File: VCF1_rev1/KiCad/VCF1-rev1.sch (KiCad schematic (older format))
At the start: 40 parts, among them U1 Opamp_Dual_Generic, U2 Opamp_Dual_Generic, U3 74HC4053, U4 CEM3350, U5 74HC4053

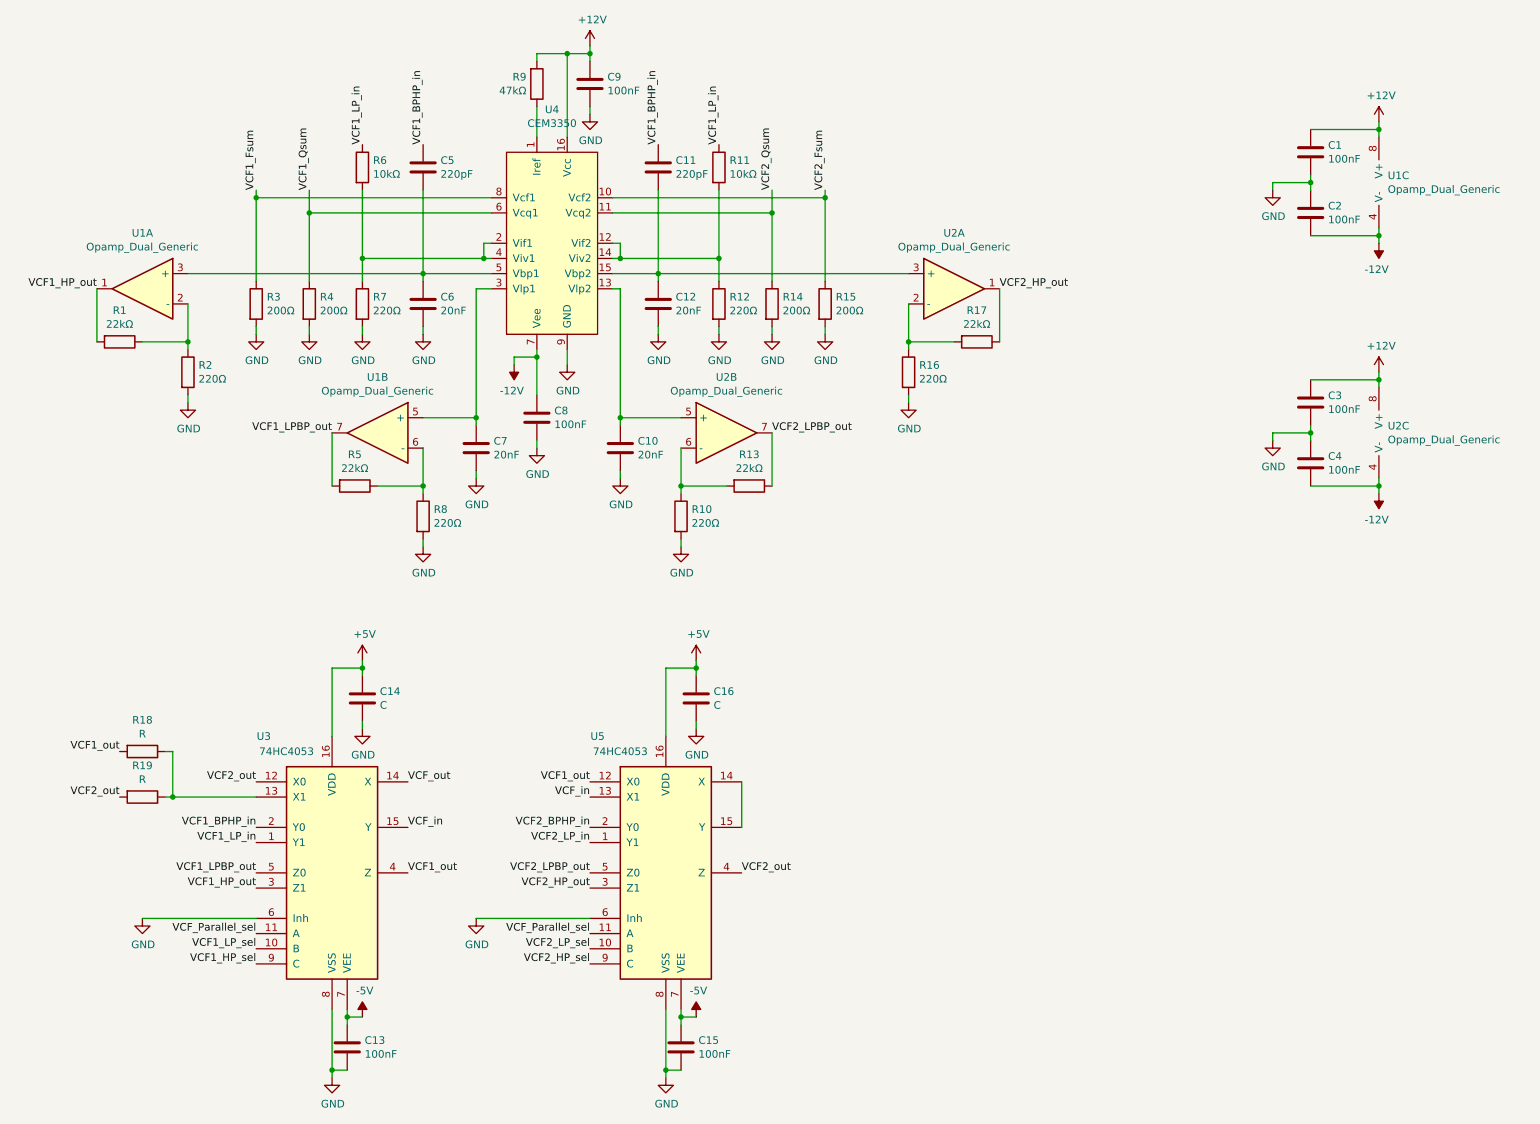
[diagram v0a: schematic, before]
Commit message: Shifted to multi page layout and also started on the panel.
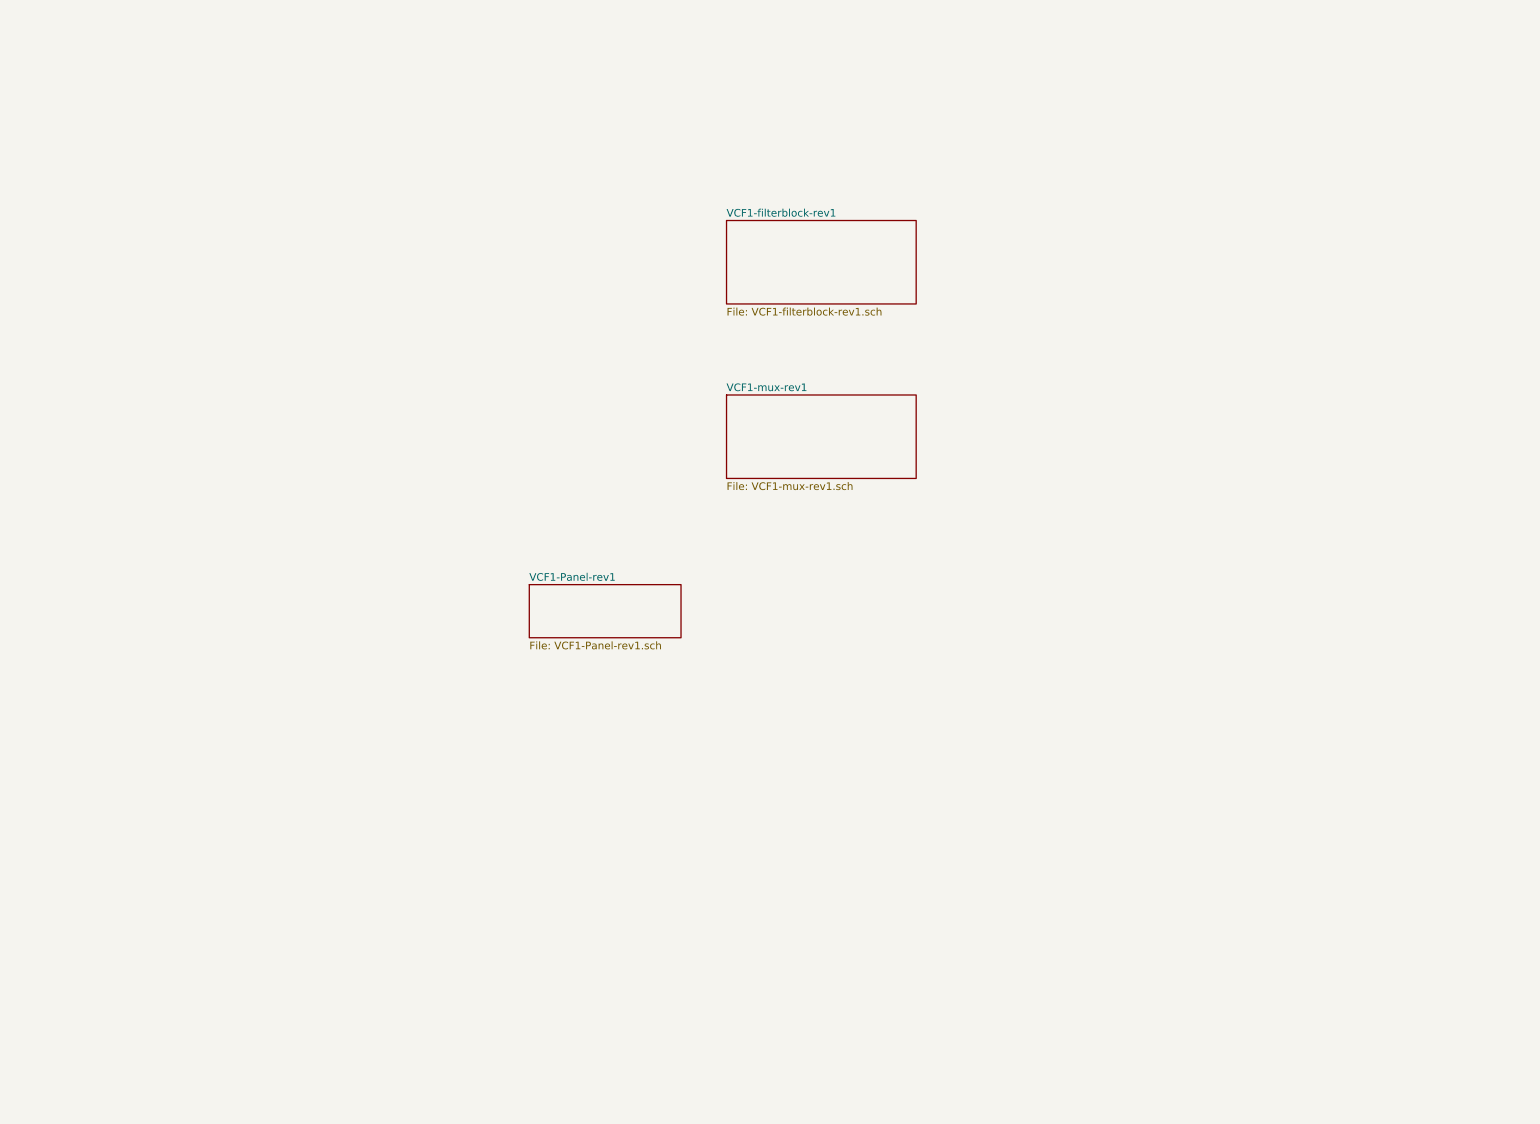
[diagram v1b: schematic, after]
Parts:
- removed C1, C13, C15, C2, C3, C4, C8, C9: 100nF, symbol Device:C
- removed C10, C12, C6, C7: 20nF, symbol Device:C
- removed C11, C5: 220pF, symbol Device:C
- removed C14, C16: C, symbol Device:C
- removed R1, R13, R17, R5: 22kΩ, symbol Device:R
- removed R10, R12, R16, R2, R7, R8: 220Ω, symbol Device:R
- removed R11, R6: 10kΩ, symbol Device:R
- removed R14, R15, R3, R4: 200Ω, symbol Device:R
- removed R18, R19: R, symbol Device:R
- removed R9: 47kΩ, symbol Device:R
- removed U1, U2: Opamp_Dual_Generic, symbol Device:Opamp_Dual_Generic
- removed U3, U5: 74HC4053, symbol 4xxx:4053
- removed U4: CEM3350, symbol ModularMayhemSymbols:CEM3350

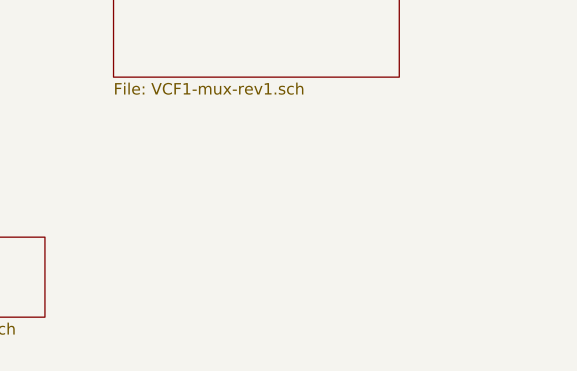
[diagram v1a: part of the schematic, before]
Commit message: Added some initial resonance control and some other stuff.
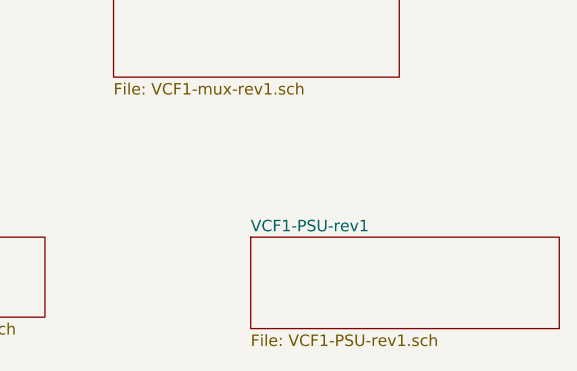
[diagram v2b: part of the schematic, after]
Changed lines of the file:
@@
 $Descr A4 11693 8268
 encoding utf-8
-Sheet 1 4
+Sheet 1 5
 Title ""
 Date ""
@@
 F1 "VCF1-Panel-rev1.sch" 50
 $EndSheet
+$Sheet
+S 5900 4300 1350 400
+U 61791AB3
+F0 "VCF1-PSU-rev1" 50
+F1 "VCF1-PSU-rev1.sch" 50
+$EndSheet
 $EndSCHEMATC
